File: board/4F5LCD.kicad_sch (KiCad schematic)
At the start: 0 parts

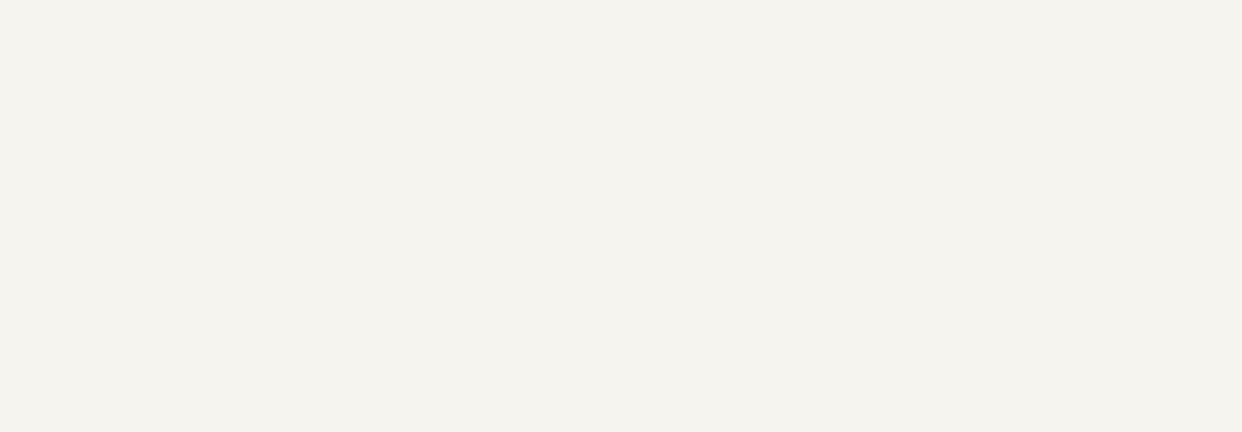
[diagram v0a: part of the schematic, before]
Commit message: Added stl and skp files for 3D printing, changed ground planes and net names, exported schematics as pdf
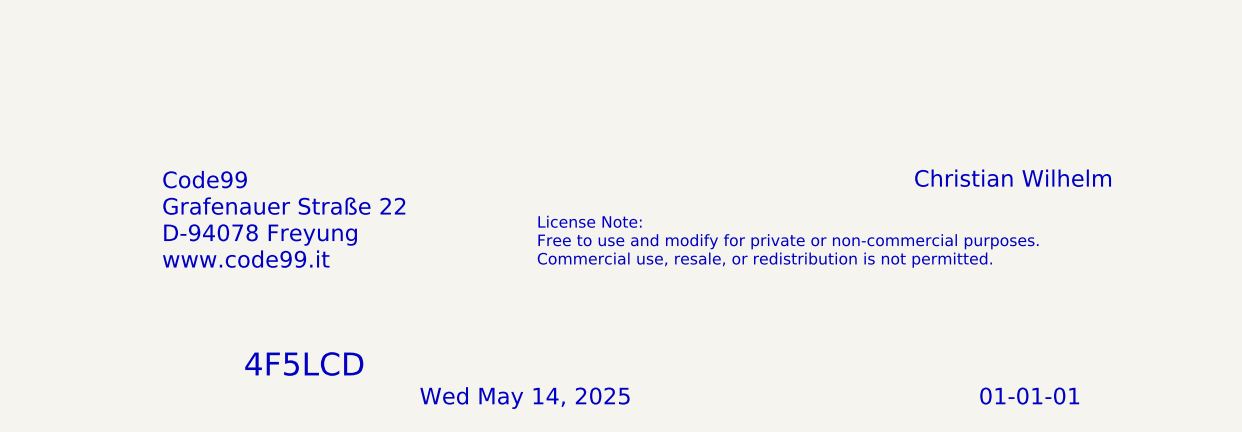
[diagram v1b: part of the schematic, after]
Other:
- note added: "01-01-01"
- note added: "4F5LCD"
- note added: "Christian Wilhelm"
- note added: "Code99 Grafenauer Straße 22 D-94078 Freyung www.code99.it"
- note added: "License Note: Free to use and modify for private or non-commercial purposes. Commercial use, resale, or redistribution is not permitted."
- note added: "Wed May 14, 2025"
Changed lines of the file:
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@@
 	(generator_version "9.0")
 	(paper "A4")
+	(text "Wed May 14, 2025"
+		(exclude_from_sim no)
+		(at 206.6683 193.346 0)
+		(effects
+			(font
+				(size 1.8288 1.8288)
+			)
+			(justify left)
+		)
+	)
+	(text "Code99\nGrafenauer Straße 22\nD-94078 Freyung\nwww.code99.it"
+		(exclude_from_sim no)
+		(at 178.054 173.736 0)
+		(effects
+			(font
+				(size 1.8288 1.8288)
+			)
+			(justify left)
+		)
+	)
+	(text "4F5LCD"
+		(exclude_from_sim no)
+		(at 187.1344 189.8105 0)
+		(effects
+			(font
+				(size 2.54 2.54)
+			)
+			(justify left)
+		)
+	)
 	(text "100: Power supply, 6...24V in, 3.3V out\n200: Microcontroller Board\n300: CAN Controllers and Transceivers\n400: Display"
 		(exclude_from_sim no)
@@
 			)
 			(justify left)
+		)
+	)
+	(text "01-01-01"
+		(exclude_from_sim no)
+		(at 268.8055 193.346 0)
+		(effects
+			(font
+				(size 1.8288 1.8288)
+			)
+			(justify left)
+		)
+	)
+	(text "Christian Wilhelm"
+		(exclude_from_sim no)
+		(at 283.718 169.164 0)
+		(effects
+			(font
+				(size 1.8288 1.8288)
+			)
+			(justify right)
+		)
+	)
+	(text "License Note:\nFree to use and modify for private or non-commercial purposes.\nCommercial use, resale, or redistribution is not permitted."
+		(exclude_from_sim no)
+		(at 219.71 176.022 0)
+		(effects
+			(font
+				(size 1.27 1.27)
+				(color 255 117 0 1)
+			)
+			(justify left)
